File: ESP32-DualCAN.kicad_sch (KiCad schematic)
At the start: 47 parts, among them J1 USB_C_Receptacle_USB2.0_14P, J2 705510040, J3 holes, J4 holes, J5 pads, SW1 Reset, SW2 Boot, U1 LV2862Y, U2 ESP32-C6-MINI-1, U3 SN65HVD230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

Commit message: Moved CAN0 pins.  Added UART tap points.
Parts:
- added J6: Aux1, Connector_PinHeader_1.00mm:PinHeader_1x06_P1.00mm_Horizontal, symbol Connector:Conn_01x06_Pin
- SW1: value Reset -> Rst
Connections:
- net +3.3V: now also J6.6 (Pin_6)
- net CAN0_RXD: now also U2.27 (IO21); no longer U2.30 (RXD0)
- net CAN0_TXD: now also U2.26 (IO20); no longer U2.31 (TXD0)
- net GND: now also J6.5 (Pin_5)
- net UART1_RX: now reaches U2.28 (IO22)
- net UART1_RX: now also J6.1 (Pin_1)
- net UART1_TX: now reaches U2.29 (IO23)
- net UART1_TX: now also J6.2 (Pin_2)
- new net UART0_RX: J6.3 (Pin_3), U2.30 (RXD0)
- new net UART0_TX: J6.4 (Pin_4), U2.31 (TXD0)
- no-connect marks 13 -> 9

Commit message: ESP32-C6-Zero main
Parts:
- removed C4, C6: 100n, Capacitor_SMD:C_0402_1005Metric, symbol Device:C_Small
- removed D1: ESDA5V3L, Package_DFN_QFN:Diodes_DFN1006-3, symbol Power_Protection:ESDA5V3L
- removed D2: DSK38, Diode_SMD:D_SOD-123F, symbol Diode:1N4148WS
- removed D5: Yellow, LED_SMD:LED_0603_1608Metric, symbol Device:LED
- removed D7, D8: H5VNT2B, Package_TO_SOT_SMD:SOT-23, symbol Device:D_TVS_Dual_AAC
- removed J1: USB_C_Receptacle_USB2.0_14P, Connector_USB:USB_C_Receptacle_GCT_USB4105-xx-A_16P_TopMnt_Horizontal, symbol Connector:USB_C_Receptacle_USB2.0_14P
- removed J6: Aux1, Connector_PinHeader_1.00mm:PinHeader_1x06_P1.00mm_Horizontal, symbol Connector:Conn_01x06_Pin
- removed R1, R2: 5.11K, Resistor_SMD:R_0402_1005Metric, symbol Device:R
- removed R10, R11, R7: 470, Resistor_SMD:R_0402_1005Metric, symbol Device:R
- removed R14, R15: 22, Resistor_SMD:R_0402_1005Metric, symbol Device:R_Small
- removed R4: 51k, Resistor_SMD:R_0402_1005Metric, symbol Device:R_Small
- removed R5, R6: 10k, Resistor_SMD:R_0402_1005Metric, symbol Device:R_Small
- removed SW1: Rst, Button_Switch_SMD:SW_SPST_TS-1088-xR020, symbol Switch:SW_Push
- removed SW2: Boot, Button_Switch_SMD:SW_SPST_TS-1088-xR020, symbol Switch:SW_Push
- removed U2: ESP32-C6-MINI-1, RF_Module:ESP32-C6-MINI-1, symbol RF_Module:ESP32-C6-MINI-1
- added J2, J3: Conn_01x10_Socket, Connector_PinSocket_2.54mm:PinSocket_1x10_P2.54mm_Vertical, symbol Connector:Conn_01x10_Socket
- added J7: pads, symbol Connector:Conn_01x06_Socket
- added U2: ESP32-C6-Zero, Waveshare-ESP32:Waveshare-ESP32-C6-Zero, symbol esp:Waveshare-ESP32-C6-Zero
- added U5: ESP32-C6-SuperMini, symbol esp:ESP32-C6-SuperMini
- J1: renamed from J2; value 705510040 -> Molex 70553 6p; footprint lib:CONN_70551-xxxx_06_MOL -> lib:CONN_705530005_06_MOL; LCSC C17342575 -> C505298
- J5: footprint Connector_Wire:SolderWire-0.1sqmm_1x06_P3.6mm_D0.4mm_OD1mm -> (none)
- R8: value 51k -> 68k; LCSC C25794 -> C36871
- R9: value 15k -> 12k; LCSC C25756 -> C25752
- U3, U4: value SN65HVD230 -> TCAN1044AV; symbol Interface_CAN_LIN:SN65HVD230 -> Interface_CAN_LIN:TJA1049T-3; LCSC C12084 -> C3234993
- renumbered J3 to J4, J4 to J6
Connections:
- net +3.3V: now also U3.5 (VIO), U4.5 (VIO), J2.3 (Pin_3), U2.3 (V3V), U5.3 (V3V); no longer C12.1, C13.1, C5.1, C8.1, C9.1, L1.2, R8.2, U3.3 (VCC), U4.3 (VCC)
- net +BATT: now also J7.1 (Pin_1)
- net CAN0_H: now also J7.5 (Pin_5)
- net CAN0_L: now also J7.6 (Pin_6)
- net CAN0_RS: now also J3.5 (Pin_5), U2.14 (IO18), U5.16 (IO2)
- net CAN0_RXD: now also U3.4 (RXD), J2.4 (Pin_4), U2.4 (IO0), U5.4 (IO20)
- net CAN0_TXD: now also J2.5 (Pin_5), U2.5 (IO1), U5.5 (IO19)
- net CAN1_H: now also J7.4 (Pin_4)
- net CAN1_L: now also J7.3 (Pin_3)
- net CAN1_RS: now also J3.6 (Pin_6), U2.13 (IO19), U5.15 (IO3)
- net CAN1_RXD: now also U4.4 (RXD), J2.6 (Pin_6), U2.6 (IO2), U5.6 (IO18)
- net CAN1_TXD: now also J2.7 (Pin_7), U2.7 (IO3), U5.7 (IO15)
- net GND: now also J2.2 (Pin_2), J3.10 (Pin_10), J7.2 (Pin_2), U2.2 (GND), U5.11 (IO7), U5.2 (GND)
- new net: J2.8 (Pin_8), U2.8 (IO4)
- new net: J2.9 (Pin_9), U2.9 (IO5)
- new net: J3.9 (Pin_9), U2.10 (IO22)
- new net: J3.8 (Pin_8), U2.11 (IO21)
- new net: J3.7 (Pin_7), U2.12 (IO20)
- new net: J3.4 (Pin_4), U2.15 (IO15)
- new net: J3.3 (Pin_3), U2.16 (IO14)
- new net: J3.2 (Pin_2), U2.17 (RX)
- new net: J3.1 (Pin_1), U2.18 (TX)
- new net +5V: C12.1, C13.1, C5.1, C8.1, C9.1, J2.1 (Pin_1), L1.2, R8.2, U2.1 (VCC), U3.3 (VCC), U4.3 (VCC), U5.1 (VCC)
- no-connect marks 9 -> 2
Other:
- note added: "VOUT = 0.765V (1+(R1/R2))=4.95V"
- note removed: "Delay"
- note removed: "VOUT = 0.765V (1+(R1/R2))=3.366V"
- moved on the sheet: C12, C13, J1, J4, J5, J6, R12, U3, U4

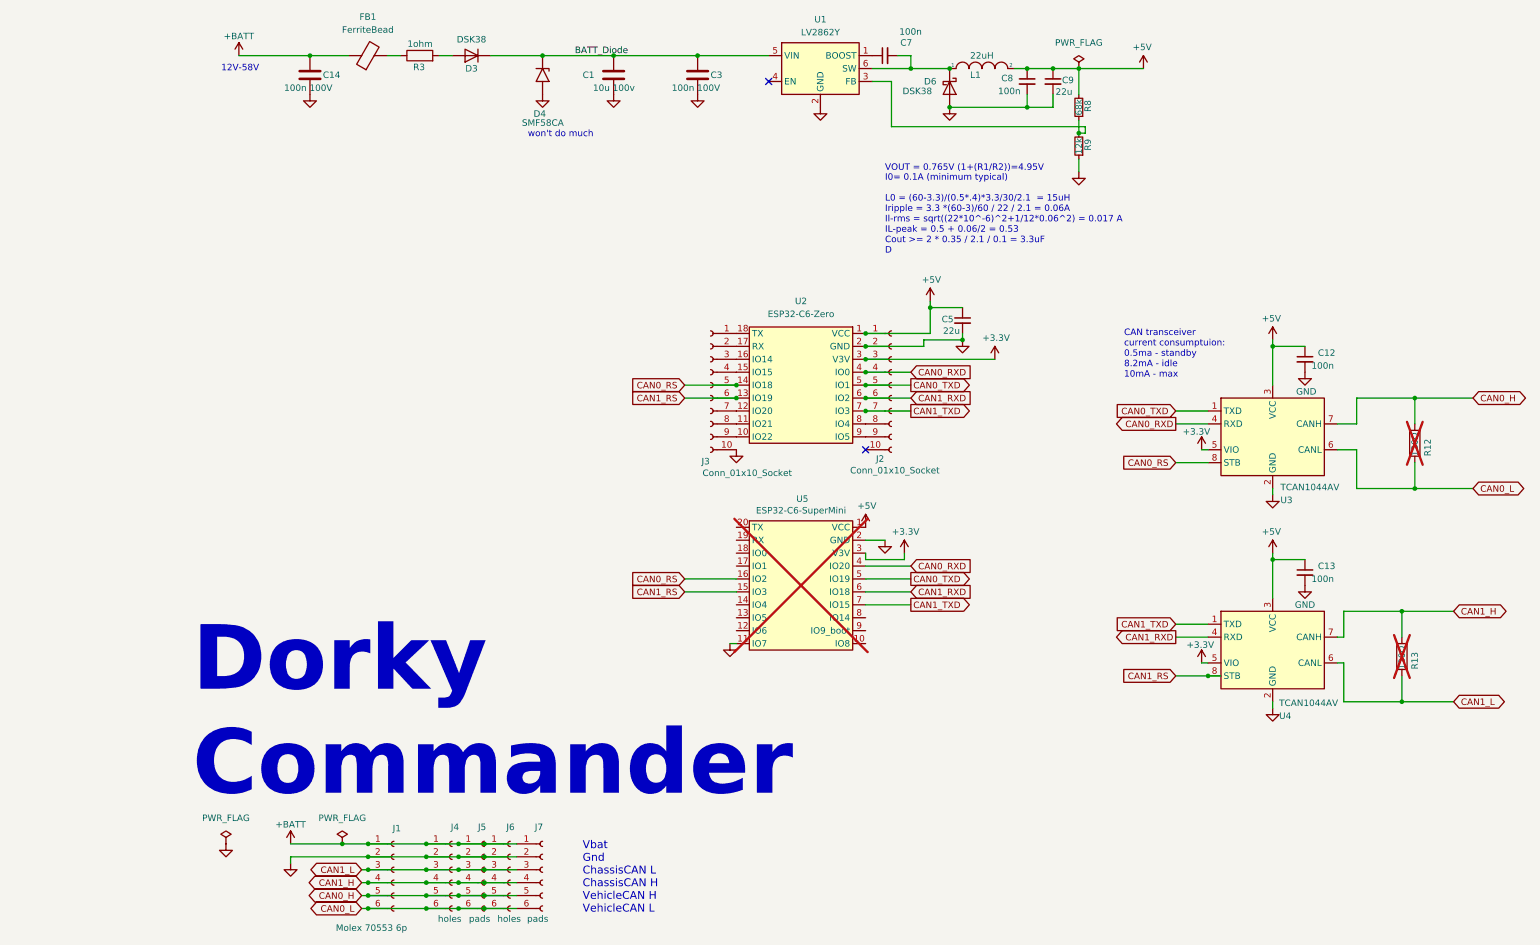
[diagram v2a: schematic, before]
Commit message: ESP32-C6-SuperMini as main
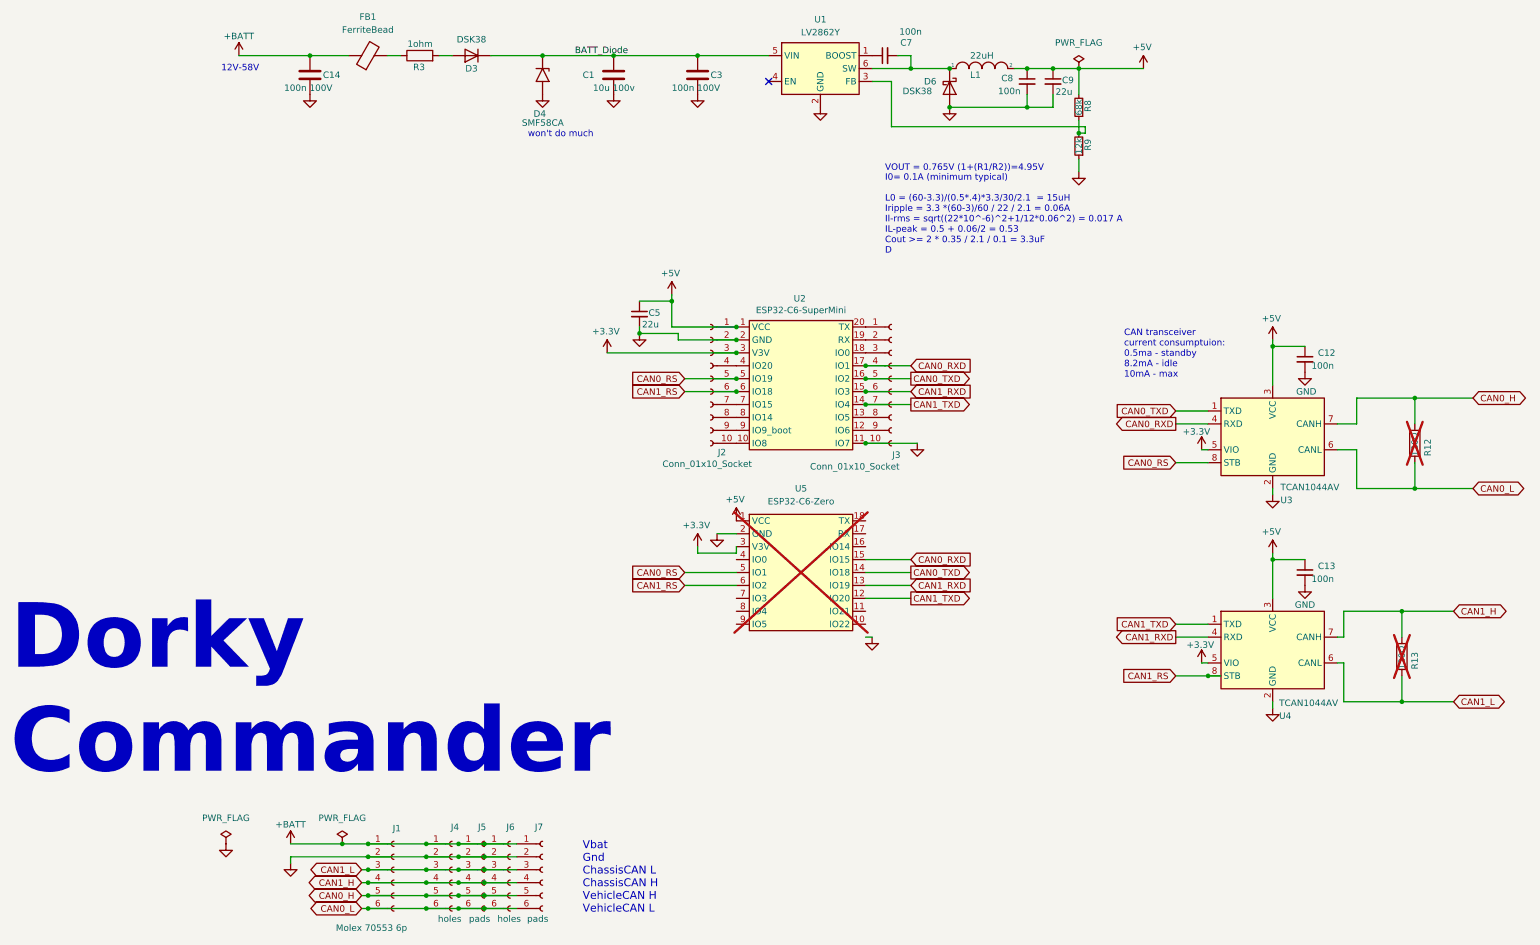
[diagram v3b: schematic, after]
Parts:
- J2, J3: LCSC (none) -> C2905418; now left out of the parts list
- U2: renamed from U5; footprint (none) -> lib:ESP32-C6-SuperMini; now fitted
- U5: renamed from U2; now not fitted
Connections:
- net CAN0_RS: now also J2.5 (Pin_5), U2.5 (IO19), U5.5 (IO1); no longer J3.5 (Pin_5), U2.16 (IO2), U5.14 (IO18)
- net CAN0_RXD: now also J3.4 (Pin_4), U2.17 (IO1), U5.15 (IO15); no longer J2.4 (Pin_4), U2.4 (IO20), U5.4 (IO0)
- net CAN0_TXD: now also J3.5 (Pin_5), U2.16 (IO2), U5.14 (IO18); no longer J2.5 (Pin_5), U2.5 (IO19), U5.5 (IO1)
- net CAN1_RS: now also J2.6 (Pin_6), U2.6 (IO18), U5.6 (IO2); no longer J3.6 (Pin_6), U2.15 (IO3), U5.13 (IO19)
- net CAN1_RXD: now also J3.6 (Pin_6), U2.15 (IO3), U5.13 (IO19); no longer J2.6 (Pin_6), U2.6 (IO18), U5.6 (IO2)
- net CAN1_TXD: now also J3.7 (Pin_7), U2.14 (IO4), U5.12 (IO20); no longer J2.7 (Pin_7), U2.7 (IO15), U5.7 (IO3)
- net at J2.10 (Pin_10): now also U2.10 (IO8)
- net at J2.8 (Pin_8): now also U2.8 (IO14); no longer U5.8 (IO4)
- net at J2.9 (Pin_9): now also U2.9 (IO9_boot); no longer U5.9 (IO5)
- net at U2.12 (IO6): now also J3.9 (Pin_9)
- net at U2.13 (IO5): now also J3.8 (Pin_8)
- net at U2.18 (IO0): now also J3.3 (Pin_3)
- net at U2.19 (RX): now also J3.2 (Pin_2)
- net at U2.20 (TX): now also J3.1 (Pin_1)
- net at U5.10 (IO22): no longer J3.9 (Pin_9)
- net at U5.11 (IO21): no longer J3.8 (Pin_8)
- net at U5.16 (IO14): no longer J3.3 (Pin_3)
- net at U5.17 (RX): no longer J3.2 (Pin_2)
- net at U5.18 (TX): no longer J3.1 (Pin_1)
- new net: J2.4 (Pin_4), U2.4 (IO20)
- new net: J2.7 (Pin_7), U2.7 (IO15)
- no-connect marks 2 -> 1
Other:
- moved on the sheet: C5, J2, J3

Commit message: cleanup
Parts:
- U5: now fitted
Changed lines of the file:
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@@
 	(generator_version "9.0")
 	(paper "A4")
+	(rectangle
+		(start 100.33 107.95)
+		(end 172.72 139.7)
+		(stroke
+			(width 0)
+			(type dash)
+		)
+		(fill
+			(type none)
+		)
+	)
 	(text "12V-58V"
 		(exclude_from_sim no)
@@
 	(text "Dorky\nCommander"
 		(exclude_from_sim no)
-		(at -19.558 148.844 0)
+		(at 18.796 149.352 0)
 		(effects
 			(font
@@
 	(wire
 		(pts
-			(xy 148.59 138.43) (xy 149.86 138.43)
-		)
-		(stroke
-			(width 0)
-			(type default)
-		)
-	)
-	(wire
-		(pts
 			(xy 214.63 143.51) (xy 215.9 143.51)
 		)
@@
 	)
 	(symbol
-		(lib_id "power:GND")
-		(at 149.86 138.43 0)
-		(unit 1)
-		(exclude_from_sim no)
-		(in_bom yes)
-		(on_board yes)
-		(dnp no)
-		(property "Reference" "#PWR015"
-			(at 149.86 144.78 0)
-			(effects
-				(font
-					(size 1.27 1.27)
-				)
-				(hide yes)
-			)
-		)
-		(property "Value" "GND"
-			(at 151.13 140.97 0)
-			(effects
-				(font
-					(size 1.27 1.27)
-				)
-				(justify left)
-				(hide yes)
-			)
-		)
-		(property "Footprint" ""
-			(at 149.86 138.43 0)
-			(effects
-				(font
-					(size 1.27 1.27)
-				)
-				(hide yes)
-			)
-		)
-		(property "Datasheet" ""
-			(at 149.86 138.43 0)
-			(effects
-				(font
-					(size 1.27 1.27)
-				)
-				(hide yes)
-			)
-		)
-		(property "Description" ""
-			(at 149.86 138.43 0)
-			(effects
-				(font
-					(size 1.27 1.27)
-				)
-				(hide yes)
-			)
-		)
-		(pin "1"
-		)
-		(instances
-			(project "ESP32-DualCAN"
-				(path "/a48c7dca-4b22-4e27-9aac-33c63a3c6130"
-					(reference "#PWR015")
-					(unit 1)
-				)
-			)
-		)
-	)
-	(symbol
 		(lib_id "Connector:Conn_01x06_Socket")
 		(at 67.31 184.15 0)
@@
 		(in_bom no)
 		(on_board no)
-		(dnp yes)
+		(dnp no)
 		(property "Reference" "U5"
 			(at 135.89 109.22 0)
